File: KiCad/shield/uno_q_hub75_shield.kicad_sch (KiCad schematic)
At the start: 0 parts

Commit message: Rebuild all schematics as valid KiCad 10 format (version 20260326)
Complete rewrite from scratch using Python generator (kicad10_gen.py).
All 16 files verified parseable with kicad-skip and structurally
compliant with the KiCad schematic file format specification.

Format compliance per dev-docs.kicad.org/en/file-formats/sexpr-schematic/:
  - version 20260326 (KiCad 10 SEXPR_SCHEMATIC_FILE_VERSION)
  - generator_version 10.0.0
  - Root (uuid) in every schematic file header
  - Every symbol instance has: (uuid UUID) + (instances (project NAME (path /ROOT/SHEET (reference REF)(unit N))))
  - Every hierarchical_label has: (uuid UUID)
  - Every sheet block has: (uuid UUID) + (instances (project NAME (path /ROOT_UUID (page N))))
  - Every sheet pin has: (uuid UUID)
  - Every text element has: (uuid UUID)
  - Root schematics have: (sheet_instances (path '/' (page '1')))
  - lib_symbols: pin type uses 'TYPE line' format (e.g. 'input line')
  - All property effects use correct KiCad 10 token syntax
  - Stable UUIDs via seed files (shield_uuids.json, carrier_uuids.json)

Shield (8 files, stable root UUID: bc84562d-846a-4607-81a1-500b7991d137):
  uno_q_hub75_shield.kicad_sch      root, 7 hierarchical sheets
  sheets/power.kicad_sch            AMS1117-3.3 LDO, FB1, indicators (17 syms)
  sheets/esp32s3.kicad_sch          ESP32-S3-WROOM-1-N16R8, USB-C (9 syms)
  sheets/hub75_driver.kicad_sch     SN74HCT245PW x2, HUB75 IDC (10 syms)
  sheets/audio_codec.kicad_sch      ES8388, DC-block caps, J_OUT/J_MIC (19 syms)
  sheets/display.kicad_sch          FPC_22pin, GT911 pullups, JP1 (7 syms)
  sheets/uno_q_interface.kicad_sch  J2 SPI3, J3 UART debug (2 syms)
  sheets/connectivity.kicad_sch     Qwiic x2, Grove x5 (10 syms)

Carrier (8 files, stable root UUID: a7d62ed3-8e95-4e64-b6df-722c91664a1a):
  uno_q_super_carrier.kicad_sch     root, 10 hierarchical sheets
  sheets/power.kicad_sch            TPS54331DR buck, AMS1117, dual VIN/HUB75 (33 syms)
  sheets/uno_q_mounting.kicad_sch   B1 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
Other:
- sheet Audio Codec ports: added AVDD; removed none
- sheet Power ports: added AVDD; removed none
- note added: "UNO Q HUB75 SHIELD — Rev 0.3 — BLOCK DIAGRAM\n\nSignal flow (IEEE 315: left to right, power top to bottom):\n\n J4 (+5V_EXT) → [POWER] → +3V3 (AMS1117) +5V_EXT_HUB75 (direct)\n J2 (UNO Q JSPI) → [UNO Q INTERFACE] → SPI3 slave to ESP32-S3\n [ESP32-S3] → HUB75 GPIO → [HUB75 DRIVER] → J1 IDC → Panel\n [ESP32-S3] → I2S → [AUDIO CODEC] → J_OUT line-out / J_MIC mic\n [ESP32-S3] → SPI2 + I2C → [DISPLAY]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"
- note removed: "UNO Q HUB75 SHIELD — Rev 0.3 — BLOCK DIAGRAM Signal flow (IEEE 315: left to right, power top to bottom): J4 (+5V_EXT) ──> [POWER] ──> +3V3 (AMS1117), +5V_EXT_HUB75 (direct) J2 (UNO Q JSPI) ──> [UNO Q INTERFACE] ──> SPI3 slave to ESP32-S3 [ESP32-S3] ──> HUB75 GPIO ──> [HUB75 DRIVER] ──> J1 IDC ──> Panel [ESP32-S3] ──> I2S ──> [AUDIO CODEC] ──> J_LINEOUT / J_MIC [ESP32-S3] ──> SPI2 + I2C ──> [DISPL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"

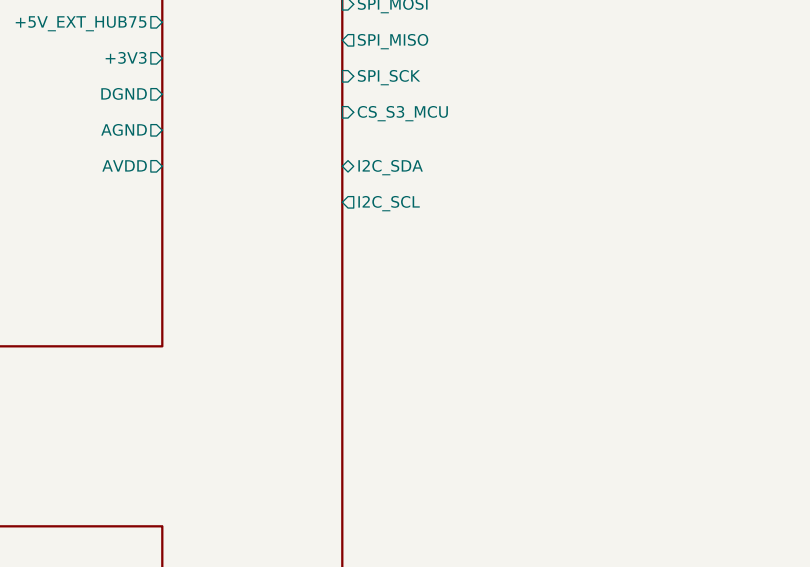
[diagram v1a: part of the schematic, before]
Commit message: Fix hierarchy mismatches — all 16 files fully audited and clean
Issues found and fixed by full-depth structural audit:

1. esp32s3.kicad_sch (shared sheet used by both boards):
   Missing 3 carrier-specific hierarchical labels:
     + CS_S3_MPU (GPIO0, carrier-only QRB2210 chip select)
     + S3_C6_TX  (S3→C6 direct UART, carrier-only)
     + S3_C6_RX  (C6→S3, carrier-only)
   These labels are valid in the shield context too (NC at shield level)
   Shield root + carrier root now both declare all 37 pins correctly

2. carrier/uno_q_super_carrier.kicad_sch (root):
   esp32s3 sheet block: missing LCD_*/TOUCH_INT pins (7 pins)
   These were declared in the shield root but dropped from carrier root
   All 37 pins now declared, matching all 37 hierarchical labels exactly

3. Net name mismatch: '+5V_HUB75' vs '+5V_EXT_HUB75'
   carrier/sheets/power.kicad_sch label: +5V_HUB75 → +5V_EXT_HUB75
   Now matches HUB75 driver sheet and carrier root declaration

Final audit results (full-depth parenthesis parsing, not window-based):
  16/16 files pass all structural checks:
  version 20260326, generator_version 10.0.0, header uuid,
  sheet_instances with path '/', symbol instances (uuid+instances),
  hierarchical_labels (uuid), sheet blocks (uuid+instances),
  sheet pins (uuid), text elements (uuid), lib pin 'TYPE line' format,
  zero duplicate UUIDs, all 17 sheet hierarchy pin↔label pairs match exactly
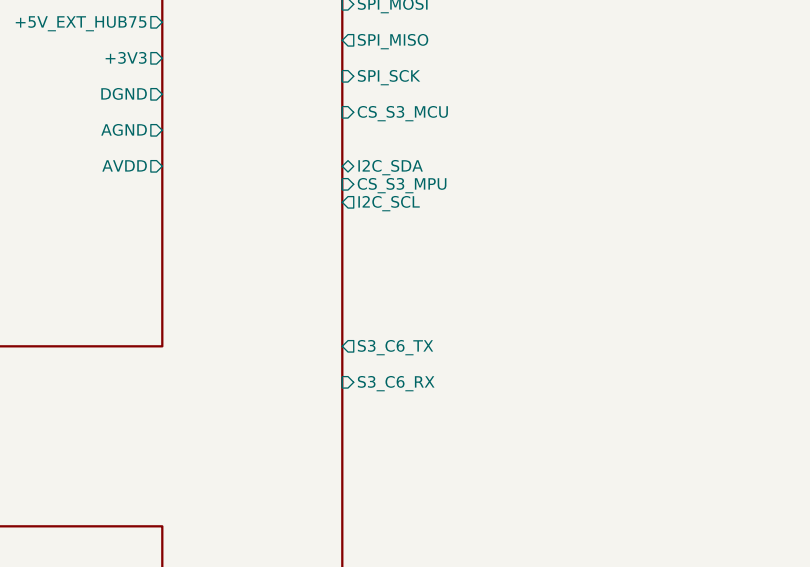
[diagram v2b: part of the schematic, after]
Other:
- sheet ESP32-S3 ports: added CS_S3_MPU, S3_C6_RX, S3_C6_TX; removed none
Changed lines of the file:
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@@
       (effects (font (size 1.27 1.27)))
     )
-    (instances
+        (pin "CS_S3_MPU" input
+      (at 100 62 180)
+      (effects (font (size 1.27 1.27)))
+    )
+    (pin "S3_C6_RX" input
+      (at 100 84 180)
+      (effects (font (size 1.27 1.27)))
+    )
+    (pin "S3_C6_TX" output
+      (at 100 80 180)
+      (effects (font (size 1.27 1.27)))
+    )
+(instances
       (project "uno_q_hub75_shield"
         (path "/bc84562d-846a-4607-81a1-500b7991d137"
